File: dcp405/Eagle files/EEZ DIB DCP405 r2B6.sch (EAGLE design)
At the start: 303 parts, among them IC1 LTC3864EMSE#PBF, IC10 MC33272ADR2G, IC11 LTC2050HVCS8#PBF, IC12 74AUP1G74DC.125, IC13 MCP23S17-E/SS, IC14 REF5025AIDR, IC15 TC77-5.0MCTTR, IC16 DAC8552IDGKR, IC17 SN74LVC1G3157DCKR, IC18 ADS1120IPWR, IC19 LM293D, IC2 TPS54060DGQ, IC20 MAX9141ESA, IC3 SI8641BB-B-IS1, IC4 SN74LVC1G139DCUR, IC5 MC78L05, IC6 MC79L05, IC7 SI8641BB-B-IS1, IC8 M24C32-WMN6P, IC9 MC33272ADR2G, J1 4907, J2 FCR7350R, J3 FCR7350B, K1 G6K-2F-5DC, Q1 SUD19P06-60, Q10 PSMN0R9-25YLC, Q11 PSMN0R9-25YLC, Q12 BSS84P, Q13 BTA26-600, Q14 FMMT493TA, Q15 2N7002, Q16 2N7002, Q17 2N7002, Q18 MMBT5401, Q19 MMBT5551, Q2 MMBT5401, Q20 MMBT5551, Q21 2N7002, Q3 D45H11FP, Q4 D45H11FP, Q5 FQPF11P06 or FQPF27P06, Q6 BCP56-16.115, Q7 MMBT5401, Q8 NZT605, Q9 BSS205NH6327XTSA1, X1 39-30-1020, X2 77317-104-28LF, X3 1844249, X4 DS1024-2*10R0

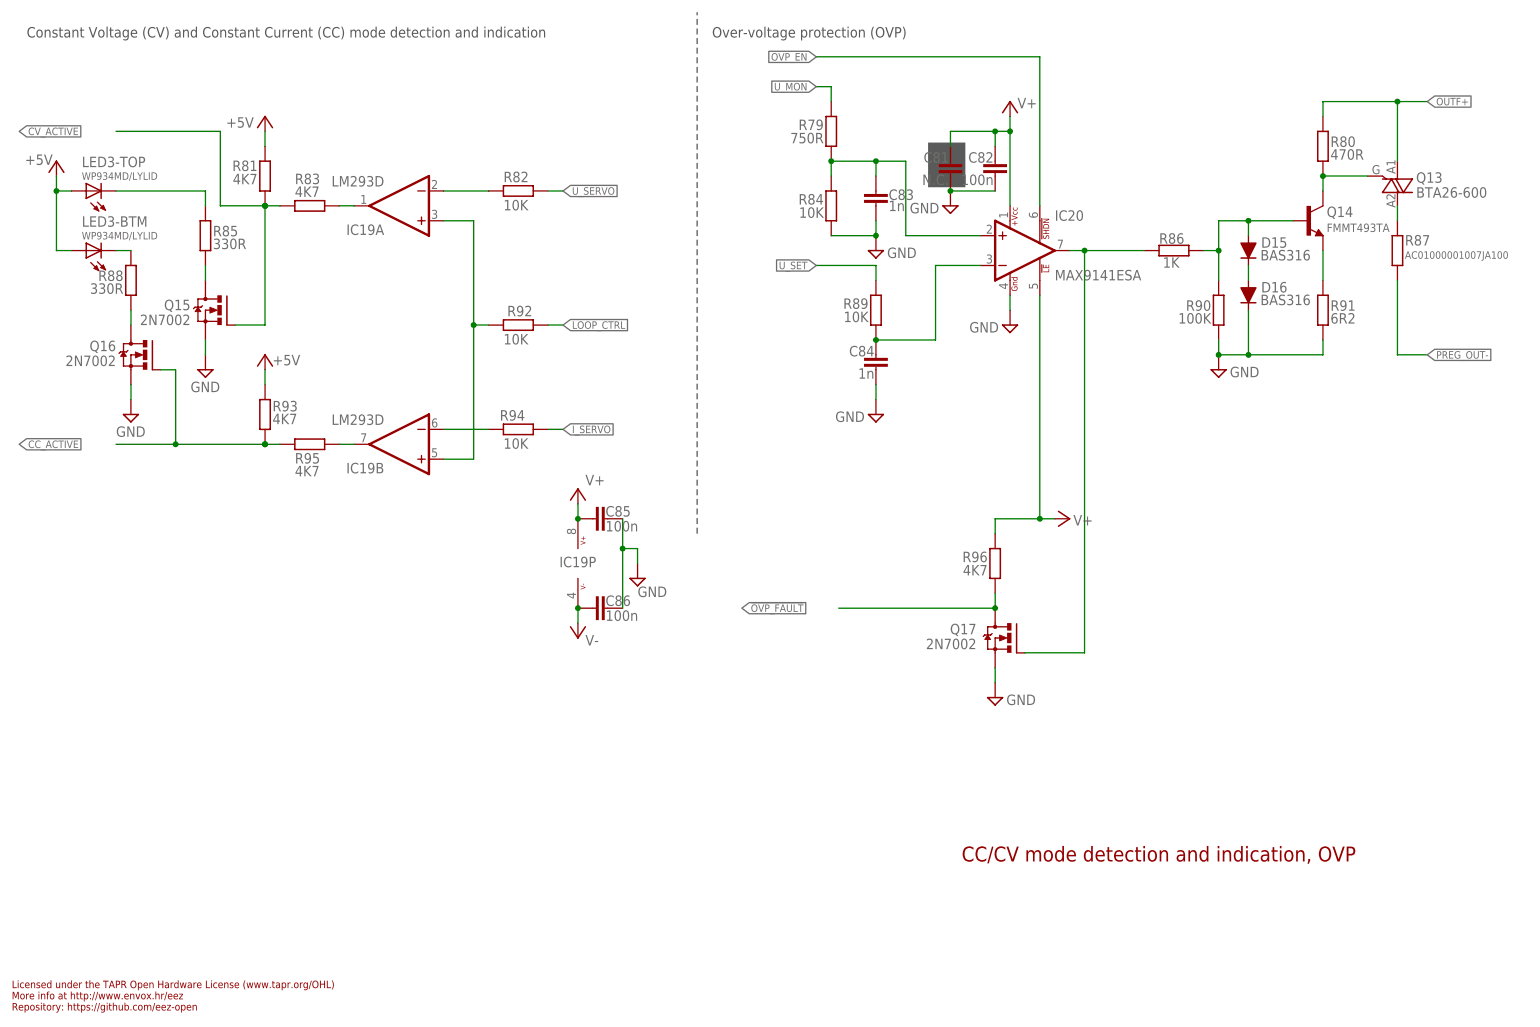
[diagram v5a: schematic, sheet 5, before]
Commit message: DCP405 BOM and front panel update
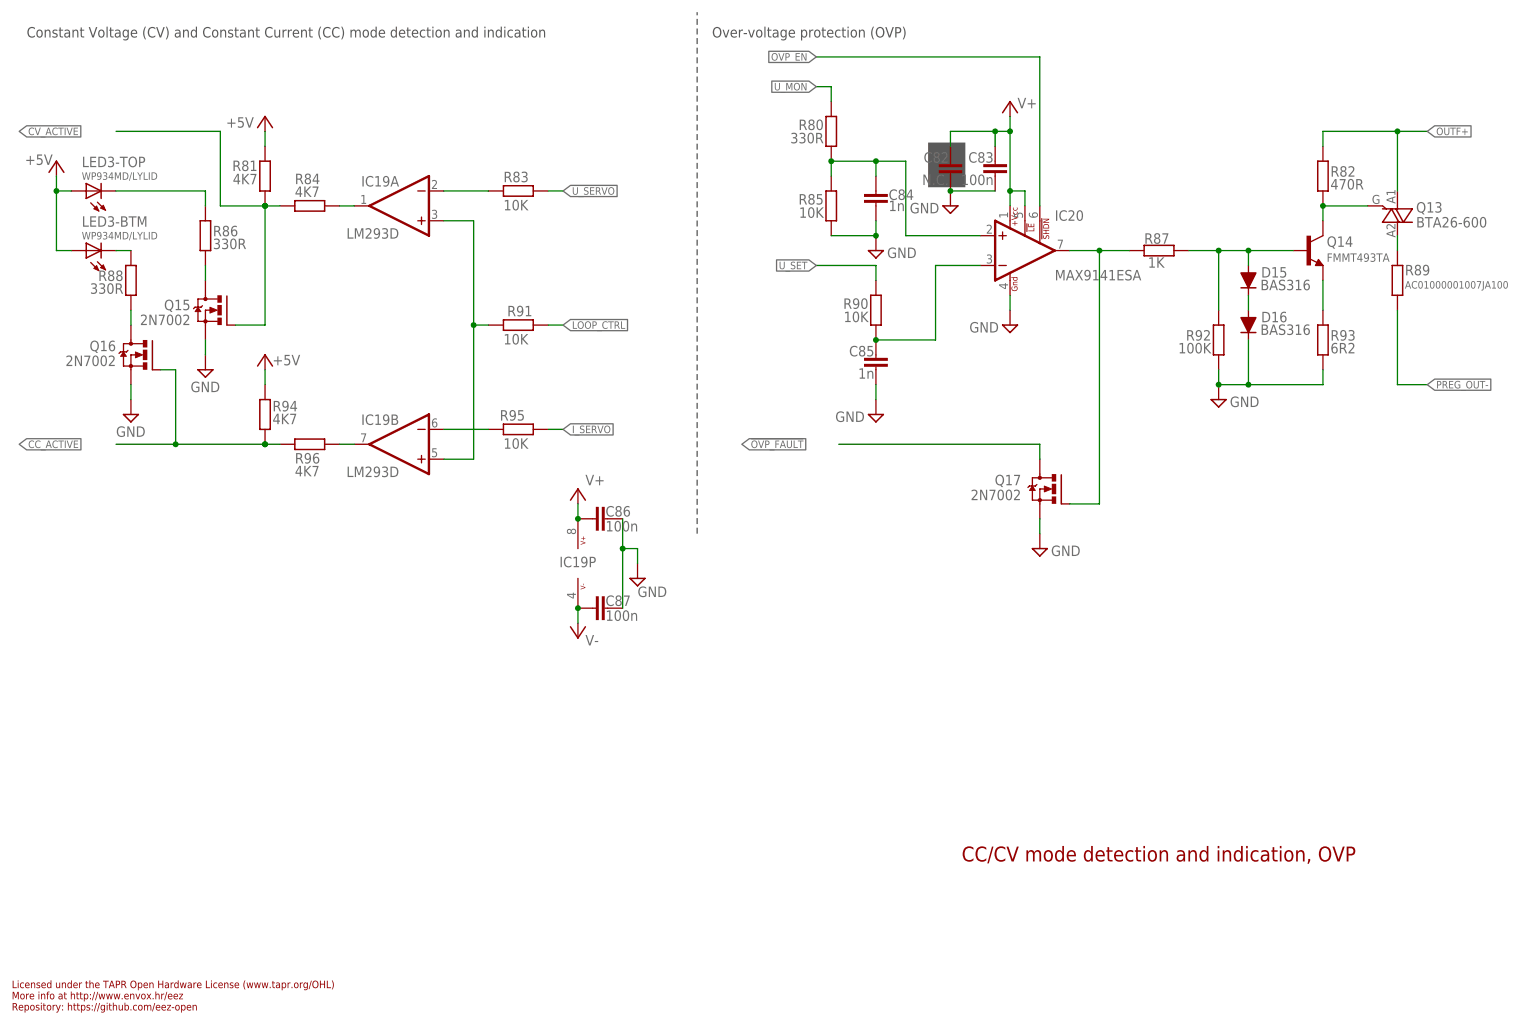
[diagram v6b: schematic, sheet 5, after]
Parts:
- added C96: 10n, rcl:C-EUC0805
- C61, C85: value 100n -> 1n; device rcl:C-EUC0603 -> rcl:C-EUC0805
- C63: value 4u7 -> 100n; device rcl:C-EUC1206 -> rcl:C-EUC0603
- C64: value 100n -> 4u7; device rcl:C-EUC0603 -> rcl:C-EUC1206
- C65: value 4u7 tant. -> 100n; device EEZ_Lib1:ECAP1206 -> rcl:C-EUC0603
- C66: value 1u -> 4u7 tant.; device rcl:C-EUC0805 -> EEZ_Lib1:ECAP1206
- C68, C78, C80: value 100n -> 1u; device rcl:C-EUC0603 -> rcl:C-EUC0805
- C71, C87: value 10n -> 100n; device rcl:C-EUC0805 -> rcl:C-EUC0603
- C72: value 4n7 -> 10n
- C76: value 100n -> 4n7; device rcl:C-EUC0603 -> rcl:C-EUC0805
- C77, C79: value 1u -> 100n; device rcl:C-EUC0805 -> rcl:C-EUC0603
- C81: value N.C. -> 100n; device rcl:C-EUC0805 -> rcl:C-EUC0603
- C82: value 100n -> N.C.; device rcl:C-EUC0603 -> rcl:C-EUC0805
- C83: value 1n -> 100n; device rcl:C-EUC0805 -> rcl:C-EUC0603
- C88: value 470n -> 10n; device rcl:C-EUC1206 -> rcl:C-EUC0805
- C89: value HHXC630A330MHA0G -> 470n; device EEZ_Lib1:ECAPSMD8.3MM/HA0 -> rcl:C-EUC1206
- C90: value 10n/200V -> HHXC630A330MHA0G; device rcl:C-EUC1206 -> EEZ_Lib1:ECAPSMD8.3MM/HA0
- C91: value N.C. -> 10n/200V; device EEZ_Lib1:ECAP2G/5 -> rcl:C-EUC1206
- C92: device rcl:C-EUC0805 -> EEZ_Lib1:ECAP2G/5
- C94: value 10n/200V -> N.C.; device rcl:C-EUC1206 -> rcl:C-EUC0805
- C95: value 10n -> 10n/200V; device rcl:C-EUC0805 -> rcl:C-EUC1206
- R67, R84, R94: value 10K -> 4K7
- R68, R90: value 100K -> 10K
- R69: value 470R -> 100K
- R70: value 270R -> 470R
- R71: value 2K2 -> 270R
- R72: value 470R -> 2K2
- R74: value 2K2 -> 470R
- R78: value 10R -> 2K2; device rcl:R-EU_R1206 -> rcl:R-EU_R0805
- R79: value 750R -> 10R; device rcl:R-EU_R0805 -> rcl:R-EU_R1206
- R80: value 470R -> 330R
- R82: value 10K -> 470R
- R83, R95: value 4K7 -> 10K
- R85: value 330R -> 10K
- R86: value 1K -> 330R
- R87: value AC01000001007JA100 -> 1K; device rcl:R-EU_0411/15 -> rcl:R-EU_R0805
- R89: value 10K -> AC01000001007JA100; device rcl:R-EU_R0805 -> rcl:R-EU_0411/15
- R91: value 6R2 -> 10K
- R92: value 10K -> 100K
- R93: value 4K7 -> 6R2
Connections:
- net !DP_DRIVE: now also R72.1; no longer R71.1
- net !OVP_FAULT: now also C61.1, R67.2; no longer R96.2
- net !SET_DP: now also R69.2; no longer R68.2
- net +5V: now also C62.2, C63.1, C65.1, C78.2, R69.1, R94.2; no longer C62.1, C64.1, C76.2, R93.2
- net +VREF: now also C66.+, C70.2, C81.2; no longer C65.+, C69.2, C80.2
- net AUX_IN: now also C72.2, R73.1; no longer C71.2, R72.1
- net CC_ACTIVE: now also R94.1, R96.2; no longer R93.1, R95.2
- net CV_ACTIVE: now also R84.2; no longer R83.2
- net CV_LED: now also R86.1; no longer R85.1
- net D_CV: now also R86.2; no longer R85.2
- net GND: now also C62.1, C65.2, C66.-, C68.2, C70.1, C71.2, C74.1, C75.2, C81.1, C82.2, C87.1, R70.1, R71.2, R85.2, R92.1, R93.1; no longer C61.1, C62.2, C65.-, C66.2, C68.1, C70.2, C71.1, C74.2, C75.1, C81.2, C82.1, R69.1, R70.2, R84.2, R90.1, R91.1
- net I_MON: now also R78.1; no longer R77.1
- net I_SERVO: now also R95.1; no longer R94.1
- net I_SET: now also R75.1; no longer R74.1
- net LOOP_CTRL: now also R91.2; no longer R92.2
- net N$105: now also R84.1; no longer R83.1
- net N$106: now also R96.1; no longer R95.1
- net N$107: now also C88.2; no longer C87.2
- net N$110: now also C96.1; no longer C95.1
- net N$113: now also C89.2; no longer C88.2
- net N$12: now also R71.1; no longer R70.1
- net N$121: now also R70.2; no longer R69.2
- net N$13: now also R87.2; no longer R86.2
- net N$15: now also R89.2; no longer R87.2
- net N$153: now also R83.2; no longer R82.2
- net N$161: now also R95.2; no longer R94.2
- net N$17: now also R73.2, R74.1; no longer R72.2, R73.1
- net N$170: now also R91.1; no longer R92.1
- net N$18: now also R82.1; no longer R80.1
- net N$19: now also R93.2; no longer R91.2
- net N$21: now also R87.1, R92.2; no longer R86.1, R90.2
- net N$31: now also C85.2, R90.2; no longer C84.2, R89.2
- net N$32: now also R74.2; no longer R73.2
- net N$33: now also C84.2, R80.2, R85.1; no longer C83.2, R79.2, R84.1
- net N$42: now also R72.2; no longer R71.2
- net N$56: now also R68.2; no longer R67.2
- net N$70: now also C80.2, R79.2; no longer C78.2, R78.2
- net N$71: now also C68.1; no longer C67.1
- net N$72: now also C73.2, R75.2; no longer C72.2, R74.2
- net N$73: now also C76.2, R77.2; no longer C75.2, R76.2
- net N$80: now also C74.2, R76.2; no longer C73.2, R75.2
- net N$81: now also C75.1, R78.2; no longer C74.1, R77.2
- net OUTC+: now also C91.1, C92.+, C94.1; no longer C90.1, C91.+, C92.1
- net OUTC-: now also C92.-, C95.2; no longer C91.-, C92.2
- net OUTF+: now also R82.2; no longer R80.2
- net PE: now also C91.2, C95.1; no longer C90.2, C94.1
- net POST_OUT-: now also C90.-, C96.2; no longer C89.-, C95.2
- net POST_OUTF+: now also C89.1, C90.+; no longer C87.1, C89.+
- net PREG_OUT-: now also R89.1; no longer R87.1
- net U_MON: now also R77.1, R80.1; no longer R76.1, R79.1
- net U_SERVO: now also R83.1; no longer R82.1
- net U_SET: now also R76.1, R90.1; no longer R75.1, R89.1
- net V+: now also C64.1, C67.1, C69.2, C71.1, C82.1, C83.2, C86.2, R79.1; no longer C63.1, C66.1, C68.2, C70.1, C81.1, C82.2, C85.2, R78.1, R96.1
- net V-: now also C87.2; no longer C86.2
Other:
- note added: "DCP405"
- note added: "DCP405B"
- note removed: "Direction"
- moved on the sheet: C61, C62, C63, C64, C67, C68, C69, C70, C71, C72, C73, C74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

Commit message: DCP405 BOM update
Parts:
- added FM3: FIDUCIAL_2, EEZ_Lib1:FIDUCIAL_2
- C60: value 120p -> 330p
- Q3, Q4: device EEZ_Lib1:D45H11-VERT -> EEZ_Lib1:D45H11-FPV
- Q5: device EEZ_Lib1:P-MOSFET-VERT -> EEZ_Lib1:P-MOSFET-FPV
- R6: value 100R -> 15R; device rcl:R-EU_R0805 -> rcl:R-EU_R1206
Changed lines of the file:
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@@
 <part name="C49" library="rcl" deviceset="C-EU" device="C0603" value="100n"/>
 <part name="C56" library="rcl" deviceset="C-EU" device="C0603" value="100n"/>
-<part name="Q5" library="EEZ_Lib1" deviceset="P-MOSFET" device="-VERT" value="FQPF11P06 or FQPF27P06"/>
+<part name="Q5" library="EEZ_Lib1" deviceset="P-MOSFET" device="-FPV" value="FQPF11P06 or FQPF27P06"/>
 <part name="IC10" library="EEZ_Lib1" deviceset="TL072" device="SOIC8" value="MC33272ADR2G"/>
 <part name="P-1" library="supply2" deviceset="V-" device=""/>
@@
 <part name="C17" library="rcl" deviceset="C-EU" device="C0805" value="120p"/>
 <part name="C7" library="rcl" deviceset="C-EU" device="C1206" value="1u/100V"/>
-<part name="R6" library="rcl" deviceset="R-EU_" device="R0805" value="100R"/>
+<part name="R6" library="rcl" deviceset="R-EU_" device="R1206" value="15R"/>
 <part name="L3" library="EEZ_inductors_and_transformers" deviceset="COILCRAFT_HPI0630" device="" value="VLS6045AF-3R3N"/>
 <part name="SH3" library="EEZ_Lib1" deviceset="SHORT" device="NOHOLE" value="Sgnd to Pgnd short"/>
@@
 <part name="OE" library="EEZ_Lib1" deviceset="JP2-NOCUT" device=""/>
 <part name="Q8" library="EEZ_Lib1" deviceset="NZT605" device="" value="NZT605"/>
-<part name="Q3" library="EEZ_Lib1" deviceset="D45H11" device="-VERT" value="D45H11FP"/>
-<part name="Q4" library="EEZ_Lib1" deviceset="D45H11" device="-VERT" value="D45H11FP"/>
+<part name="Q3" library="EEZ_Lib1" deviceset="D45H11" device="-FPV" value="D45H11FP"/>
+<part name="Q4" library="EEZ_Lib1" deviceset="D45H11" device="-FPV" value="D45H11FP"/>
 <part name="R35" library="rcl" deviceset="R-EU_" device="R1206" value="10R"/>
 <part name="R36" library="rcl" deviceset="R-EU_" device="R1206" value="10R"/>
@@
 <part name="P+6" library="supply1" deviceset="+5V" device=""/>
 <part name="R66" library="rcl" deviceset="R-EU_" device="R0805" value="1K"/>
-<part name="C60" library="rcl" deviceset="C-EU" device="C0805" value="120p"/>
+<part name="C60" library="rcl" deviceset="C-EU" device="C0805" value="330p"/>
 <part name="R72" library="rcl" deviceset="R-EU_" device="R0805" value="2K2"/>
 <part name="D14" library="EEZ_Lib1" deviceset="DIODE" device="SOD323R" value="BAS316"/>
@@
 <part name="C58" library="rcl" deviceset="C-EU" device="C0805" value="33p"/>
 <part name="C61" library="rcl" deviceset="C-EU" device="C0805" value="1n"/>
+<part name="FM3" library="EEZ_Lib1" deviceset="FIDUCIAL" device="_2"/>
 </parts>
 <sheets>
@@
 <attribute name="VALUE" x="171.958" y="86.8426" size="1.778" layer="96"/>
 </instance>
+<instance part="FM2" gate="FD" x="251.46" y="40.64" smashed="yes"/>
+<instance part="FM1" gate="FD" x="243.84" y="40.64" smashed="yes"/>
+<instance part="FM3" gate="FD" x="259.08" y="40.64" smashed="yes"/>
 </instances>
 <busses>
@@
 <attribute name="VALUE" x="191.135" y="81.28" size="1.778" layer="96" rot="MR180"/>
 </instance>
-<instance part="FM2" gate="FD" x="259.08" y="40.64" smashed="yes"/>
-<instance part="FM1" gate="FD" x="251.46" y="40.64" smashed="yes"/>
 <instance part="X2" gate="-1" x="160.02" y="167.64" smashed="yes" rot="MR0">
 <attribute name="NAME" x="166.37" y="168.529" size="1.778" layer="95" rot="MR180"/>

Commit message: DCP405 BOM update
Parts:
- removed R108: 100K, rcl:R-EU_R0805
- added D19: BAS316, EEZ_Lib1:DIODESOD323R
- added SF: JP2-NOCUT-0805, EEZ_Lib1:JP2-NOCUT-0805
- C17: value 120p -> 33p
- C18: value 4n7 -> 6n8
- D12: value SK55 -> BAS316; device EEZ_Lib1:SCHOTTKYSMB -> EEZ_Lib1:DIODESOD323R
- D13: value BAS316 -> SK55; device EEZ_Lib1:DIODESOD323R -> EEZ_Lib1:SCHOTTKYSMB
- D17: value SK10100D1-DIO -> BAS316; device EEZ_Lib1:SCHOTTKY-DUAL_A_L -> EEZ_Lib1:DIODESOD323R
- D18: value BAS316 -> SK10100D1-DIO; device EEZ_Lib1:DIODESOD323R -> EEZ_Lib1:SCHOTTKY-DUAL_A_L
- D8: value SKL14 -> N.C.
- D9: value BAS316 -> SKL14; device EEZ_Lib1:DIODESOD323R -> EEZ_Lib1:SCHOTTKYSOD123
- R10: value 10K -> 330K
- R100, R18: value 2K2 -> 10K
- R102: value 10K -> 1R
- R103: value 1R -> 750R
- R104: value 750R -> 47K
- R105: value 47K -> 330R
- R106: value 330R -> 470R
- R107: value 470R -> 100K
- R11: value 330K -> 100K
- R12, R9: value 100K -> 4K7
- R13: value 4K7 -> 10R; device rcl:R-EU_R0805 -> rcl:R-EU_R1206
- R14: value 10R -> 47K; device rcl:R-EU_R1206 -> rcl:R-EU_R0805
- R15: value 47K -> 10R; device rcl:R-EU_R0805 -> rcl:R-EU_R1206
- R17: value 10R -> 2K2; device rcl:R-EU_R1206 -> rcl:R-EU_R0805
- R19, R68, R8, R91: value 10K -> 100K
- R20: value 100K -> 330K
- R21: value 330K -> 86K6
- R22: value 86K6 -> 10K
- R26: value 10K -> 0R1/2-3W; device rcl:R-EU_R0805 -> rcl:R-EU_R2512
- R28: value 0R1/2-3W -> 4K7; device rcl:R-EU_R2512 -> rcl:R-EU_R0805
- R29: value 4K7 -> 2R2/2W; device rcl:R-EU_R0805 -> rcl:R-EU_R2512
- R30: value 2R2/2W -> 4K7; device rcl:R-EU_R2512 -> rcl:R-EU_R0805
- R31, R67, R84, R94: value 4K7 -> 10K
- R32, R83, R95: value 10K -> 4K7
- R33: value 4K7 -> 2K2
- R34, R78: value 2K2 -> 10R; device rcl:R-EU_R0805 -> rcl:R-EU_R1206
- R36: value 10R -> 5K6; device rcl:R-EU_R1206 -> rcl:R-EU_R0805
- R37: value 5K6 -> 220R
- R38: value 220R -> 1K
- R39: value 1K -> 220R
- R4: value 47K -> 1R
- R40: value 220R -> 7K5 0.1%
- R41, R50: value 7K5 0.1% -> 2K2
- R43, R51: value 2K2 -> 4K7
- R44: value 4K7 -> 124K 0.1%
- R46: value 124K 0.1% -> 10K
- R48: value 10K -> 15R; device rcl:R-EU_R0805 -> rcl:R-EU_R1206
- R49: value 15R -> 7K5 0.1%; device rcl:R-EU_R1206 -> rcl:R-EU_R0805
- R5: value 1R -> 15R; device rcl:R-EU_R0805 -> rcl:R-EU_R1206
- R52: value 4K7 -> 100K
- R53: value 100K -> 39K 0.1%
- R54: value 39K 0.1% -> 820R 0.1%
- R55: value 820R 0.1% -> 47K
- R56: value 47K -> 2K2
- R57: value 2K2 -> 1R; device rcl:R-EU_R0805 -> rcl:R-EU_R1206
- R58: value 1R -> 10K; device rcl:R-EU_R1206 -> rcl:R-EU_R0805
- R59: value 10K -> 1K
- R6: value 15R -> 10R
- R60: value 1K -> 39K 0.1%
- R61: value 39K 0.1% -> 47K
- R62: value 47K -> 0R010 (low TCR); device rcl:R-EU_R0805 -> EEZ_Lib1:R-EU_4WIRE2512
- R63: value 0R010 (low TCR) -> 2K2; device EEZ_Lib1:R-EU_4WIRE2512 -> rcl:R-EU_R0805
- R64: value 2K2 -> 820R 0.1%
- R65: value 820R 0.1% -> 1K
- R66: value 1K -> 4K7
- R69: value 100K -> 470R
- R7: value 10R -> 10K; device rcl:R-EU_R1206 -> rcl:R-EU_R0805
- R70: value 470R -> 270R
- R71: value 270R -> 2K2
- R72: value 2K2 -> 470R
- R74: value 470R -> 2K2
- R79: value 10R -> 330R; device rcl:R-EU_R1206 -> rcl:R-EU_R0805
- R80: value 330R -> 4K7
- R81: value 4K7 -> 470R
- R82: value 470R -> 10K
- R85: value 10K -> 330R
- R86: value 330R -> 1K
- R87: value 1K -> 330R
- R88: value 330R -> AC01000002207JA100; device rcl:R-EU_R0805 -> rcl:R-EU_0411/15
- R89: value AC01000001007JA100 -> 10K; device rcl:R-EU_0411/15 -> rcl:R-EU_R0805
- R92: value 100K -> 6R2
- R93: value 6R2 -> 4K7
- R96: value 4K7 -> 330R
- R97: value 330R -> 750R
- R98: value 750R -> 1K
- R99: value 1K -> 2K2
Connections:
- net !DP_DRIVE: now also D9.A, R71.1; no longer D8.A, R72.1
- net !IOEXP_RST: now also R65.2; no longer R66.2
- net !OVP_FAULT: now also D14.C, R66.2; no longer D13.C, R67.2
- net !SET_DP: now also R68.2; no longer R69.2
- net +3V3: now also R23.1; no longer R26.1
- net +5V: now also D19.C, R100.2, R18.1, R65.1, R80.2, R93.2; no longer D18.C, R101.2, R19.1, R69.1, R81.2, R94.2
- net +VNR: now also R15.1; no longer R16.1
- net +VREF: now also R31.1; no longer R32.1
- net -12V: now also R13.1, R38.2; no longer R14.1, R40.2
- net 50MA_S: now also R54.1, R57.1; no longer R55.1, R58.1
- net 5A_S: now also R62.2; no longer R63.2
- net AUX_IN: now also R72.1; no longer R73.1
- net CC_ACTIVE: now also R93.1, R95.2; no longer R94.1, R96.2
- net CC_LED: now also R87.2; no longer R88.2
- net CURR_50MA: now also R55.2; no longer R56.2
- net CURR_5A: now also R61.2; no longer R62.2
- net CV_ACTIVE: now also R80.1, R83.2; no longer R81.1, R84.2
- net CV_LED: now also R85.1; no longer R86.1
- net DARL_C: now also R33.1; no longer R36.1
- net DC_OUT: now also R14.2; no longer R15.2
- net DIB_A0: now also R25.2; no longer R26.2
- net DIB_A1: now also R24.2; no longer R25.2
- net DIB_A2: now also R23.2; no longer R24.2
- net DP_S: now also R29.1; no longer R30.1
- net D_CC: now also R87.1; no longer R88.1
- net D_CV: now also R85.2; no longer R86.2
- net FB: now also R10.2, R12.1; no longer R11.2, R13.1
- net GCOM: now also R40.1, R53.1; no longer R41.1, R54.1
- net GND: now also D10.C, D17.C, R104.1, R107.1, R16.1, R20.1, R22.1, R37.2, R52.1, R55.1, R61.1, R69.1, R70.2, R84.2, R91.1; no longer D16.C, D8.C, R105.1, R108.1, R18.1, R21.1, R23.1, R38.2, R53.1, R56.1, R62.1, R70.1, R71.2, R85.2, R93.1
- net ISENSE+: now also R53.2; no longer R55.2
- net ISENSE-: now also R60.1, R64.2; no longer R61.1, R65.2
- net I_MON: now also R58.1, R60.2, R77.1; no longer R59.1, R61.2, R78.1
- net I_SERVO: now also D12.C, R94.1; no longer D11.C, R95.1
- net I_SET: now also R56.1, R74.1; no longer R57.1, R75.1
- net LOOP_CTRL: now also D12.A, R41.1, R90.2; no longer D10.A, R43.1, R91.2
- net L_OUT: now also R10.1, R5.1, R7.1; no longer R11.1, R6.1, R9.1
- net N$1: now also R7.2; no longer R8.2
- net N$102: now also R31.2, R37.1; no longer R32.2, R38.1
- net N$105: now also R83.1; no longer R84.1
- net N$106: now also R95.1; no longer R96.1
- net N$107: now also R96.1, R97.2, R99.2; no longer R100.2, R97.1, R98.2
- net N$108: now also R101.2; no longer R102.2
- net N$109: now also R98.1; no longer R99.1
- net N$11: now also R57.2, R62.2S; no longer R58.2, R63.2S
- net N$110: now also R103.1, R105.2; no longer R104.1, R106.2
- net N$112: now also R101.1, R104.2; no longer R102.1, R105.2
- net N$113: now also R102.2; no longer R103.2
- net N$114: now also D19.A, R106.1; no longer D18.A, R107.1
- net N$12: now also R70.1; no longer R71.1
- net N$120: now also R106.2; no longer R107.2
- net N$121: now also R69.2; no longer R70.2
- net N$13: now also R86.2; no longer R87.2
- net N$14: now also R50.2; no longer R51.2
- net N$15: now also R88.2; no longer R89.2
- net N$150: now also R40.2, R44.1; no longer R41.2, R45.1
- net N$153: now also R82.2; no longer R83.2
- net N$158: now also R45.1, R49.2; no longer R46.1, R50.2
- net N$161: now also R94.2; no longer R95.2
- net N$17: now also R72.2, R73.1; no longer R73.2, R74.1
- net N$170: now also R90.1; no longer R91.1
- net N$173: now also R98.2, R99.1; no longer R100.1, R99.2
- net N$179: now also R13.2; no longer R14.2
- net N$18: now also R81.1; no longer R82.1
- net N$19: now also R92.2; no longer R93.2
- net N$2: now also R9.1; no longer R10.1
- net N$20: now also D16.C, D17.A; no longer D15.C, D16.A
- net N$200: now also R62.1S, R64.1; no longer R63.1S, R65.1
- net N$21: now also D16.A, R86.1, R91.2; no longer D15.A, R87.1, R92.2
- net N$24: now also SF.2; no longer R4.1
- net N$26: now also R16.2; no longer R17.2
- net N$28: now also R4.2; no longer R5.2
- net N$30: now also R4.1; no longer R5.1
- net N$31: now also R89.2; no longer R90.2
- net N$32: now also R73.2; no longer R74.2
- net N$33: now also R79.2, R84.1; no longer R80.2, R85.1
- net N$34: now also R14.1, R17.2; no longer R15.1, R18.2
- net N$35: now also R48.1; no longer R49.1
- net N$37: now also R59.1; no longer R60.1
- net N$38: now also R6.2; no longer R7.2
- net N$39: now also R36.1, R38.1; no longer R37.1, R39.1
- net N$40: now also R35.2; no longer R36.2
- net N$42: now also R71.2; no longer R72.2
- net N$43: now also R34.2; no longer R35.2
- net N$45: now also R36.2; no longer R37.2
- net N$47: now also R48.2; no longer R49.2
- net N$48: now also R20.2; no longer R21.2
- net N$49: now also R28.1, R32.2; no longer R29.1, R33.2
- net N$50: now also R21.2; no longer R22.2
- net N$51: now also R21.1; no longer R22.1
- net N$55: now also D10.A; no longer D9.A
- net N$56: now also D15.A, R67.2; no longer D13.A, R68.2
- net N$62: now also R19.1, R22.2; no longer R20.1, R23.2
- net N$70: now also R78.2; no longer R79.2
- net N$72: now also R74.2; no longer R75.2
- net N$73: now also R76.2; no longer R77.2
- net N$79: now also R11.1, R8.2; no longer R12.1, R9.2
- net N$8: now also R9.2; no longer R10.2
- net N$80: now also R75.2; no longer R76.2
- net N$81: now also R77.2; no longer R78.2
- net N$82: now also R56.2; no longer R57.2
- net N$83: now also R43.2, R46.2; no longer R44.2, R47.2
- net N$84: now also R47.2, R50.1, R51.2; no longer R48.2, R51.1, R52.2
- net N$88: now also R63.1; no longer R64.1
- net N$89: now also R58.2, R63.2; no longer R60.2, R64.2
- net N$90: now also R43.1; no longer R44.1
- net N$91: now also R51.1; no longer R52.1
- net N$98: now also R39.1; no longer R40.1
- net OUTF+: now also R81.2; no longer R82.2
- net PASS_E1: now also R26.2; no longer R27.2
- net PASS_E2: now also R27.2; no longer R28.2
- net POST_OE: now also R52.2; no longer R53.2
- net POST_OUT+: now also D8.A, R11.2, R28.2, R30.1; no longer R12.2, R30.2, R31.1
- net POST_OUT-: now also D13.A, D18.A, R102.1, R105.1; no longer D12.A, D17.A, R103.1, R106.1
- net POST_OUTF+: now also D18.C, R96.2; no longer D17.C, R97.2
- net PREG_IN-: now also R6.1; no longer R7.1
- net PREG_OUT+: now also D8.C, R26.1, R33.2, R5.2; no longer R28.1, R34.2, R6.2
- net PREG_OUT-: now also D13.C, R32.1, R62.1, R88.1; no longer D12.C, R33.1, R63.1, R89.1
- net PWRGOOD: now also D15.C, R18.2; no longer D14.C, R19.2
- net Q6C: now also R30.2; no longer R31.2
- net RSENSE: now also R107.2; no longer R108.2
- net SENSE+: now also R44.2, R97.1; no longer R45.2, R98.1
- net SENSE-: now also R103.2, R45.2; no longer R104.2, R46.2
- net SENSE_ERR: now also R100.1; no longer R101.1
- net SGND: now also R12.2, SF.1; no longer R13.2, R4.2
- net U_MON: now also R47.1, R49.1, R76.1, R79.1; no longer R48.1, R50.1, R77.1, R80.1
- net U_SERVO: now also D11.C, R82.1; no longer D10.C, R83.1
- net U_SET: now also R75.1, R89.1; no longer R76.1, R90.1
- net U_SET_OUT: now also R46.1; no longer R47.1
- net V+: now also R41.2, R78.1; no longer R43.2, R79.1
- net VOUT+: now also R15.2, R19.2; no longer R16.2, R20.2
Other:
- note added: "tss=3.2 ms"
- moved on the sheet: C39, C40, D10, D11, D14, D16, D8, IC10B, KK3, Q3, Q4, Q5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
